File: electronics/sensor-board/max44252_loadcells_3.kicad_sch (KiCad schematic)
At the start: 21 parts

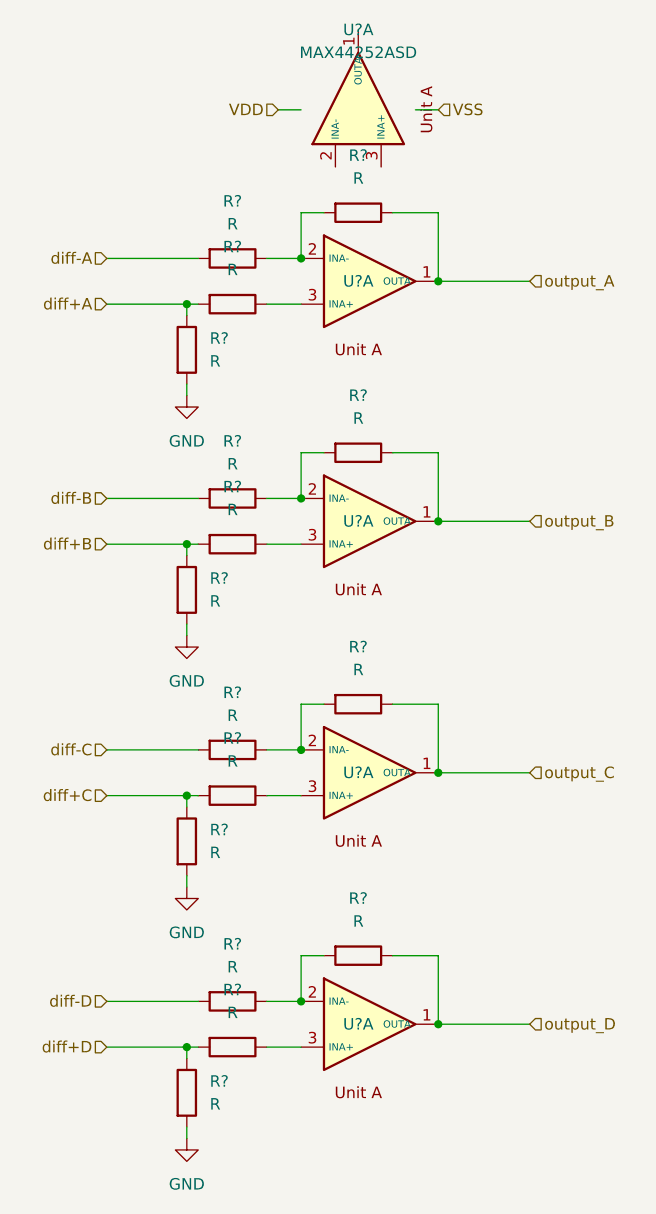
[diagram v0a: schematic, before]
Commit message: sensor-board edits
Finalized pressure and flow sensor circuits.
Reorganized schematics
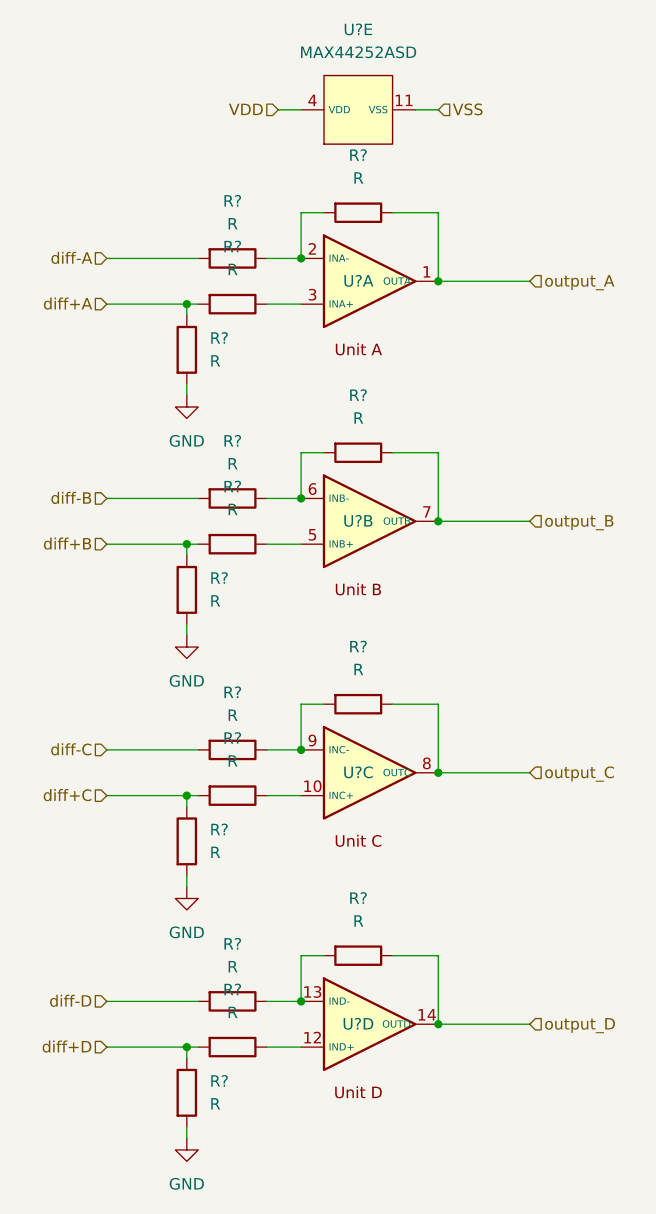
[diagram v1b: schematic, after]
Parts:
- removed R? (x16): R, symbol Device:R
- removed U? (x5): MAX44252ASD, symbol MAX44252ASD_Custom:MAX44252ASD
- added R? (x16): R, symbol Device:R
- added U? (x5): MAX44252ASD, symbol MAX44252ASD_Custom:MAX44252ASD
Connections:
- net GND: now also R?.2, R?.2, R?.2, R?.2
- net VDD: now also U?.4 (VDD)
- net VSS: now also U?.11 (VSS)
- net diff+A: now also R?.1, R?.2
- net diff+B: now also R?.1, R?.2
- net diff+C: now also R?.1, R?.2
- net diff+D: now also R?.1, R?.2
- net diff-A: now also R?.2
- net diff-B: now also R?.2
- net diff-C: now also R?.2
- net diff-D: now also R?.2
- net output_A: now also R?.1, U?.1 (OUTA)
- net output_B: now also R?.1, U?.7 (OUTB)
- net output_C: now also R?.1, U?.8 (OUTC)
- net output_D: now also R?.1, U?.14 (OUTD)
- new net: R?.1, U?.12 (IND+)
- new net: R?.1, U?.3 (INA+)
- new net: R?.1, U?.10 (INC+)
- new net: R?.1, R?.2, U?.13 (IND-)
- new net: R?.1, R?.2, U?.2 (INA-)
- new net: R?.1, R?.2, U?.9 (INC-)
- new net: R?.1, R?.2, U?.6 (INB-)
- new net: R?.1, U?.5 (INB+)
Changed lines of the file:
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@@
     (effects (font (size 1.27 1.27)) (justify left))
   )
-  (symbol (lib_id "power:GND") (at 134.62 76.2 0)
+  (symbol (lib_id "power:GND") (at 134.62 76.2 0) (unit 1)
     (in_bom yes) (on_board yes) (fields_autoplaced)
     (property "Reference" "#PWR?" (id 0) (at 134.62 82.55 0)
@@
     (pin "1")
   )
-  (symbol (lib_id "power:GND") (at 134.62 102.87 0)
+  (symbol (lib_id "power:GND") (at 134.62 102.87 0) (unit 1)
     (in_bom yes) (on_board yes) (fields_autoplaced)
     (property "Reference" "#PWR?" (id 0) (at 134.62 109.22 0)
@@
     (pin "1")
   )
-  (symbol (lib_id "power:GND") (at 134.62 130.81 0)
+  (symbol (lib_id "power:GND") (at 134.62 130.81 0) (unit 1)
     (in_bom yes) (on_board yes) (fields_autoplaced)
     (property "Reference" "#PWR?" (id 0) (at 134.62 137.16 0)
@@
     (pin "1")
   )
-  (symbol (lib_id "power:GND") (at 134.62 158.75 0)
+  (symbol (lib_id "power:GND") (at 134.62 158.75 0) (unit 1)
     (in_bom yes) (on_board yes) (fields_autoplaced)
     (property "Reference" "#PWR?" (id 0) (at 134.62 165.1 0)
@@
     (pin "1")
   )
-  (symbol (lib_id "Device:R") (at 134.62 71.12 0)
+  (symbol (lib_id "Device:R") (at 134.62 71.12 0) (unit 1)
     (in_bom yes) (on_board yes) (fields_autoplaced)
     (property "Reference" "R?" (id 0) (at 137.16 69.8499 0)
@@
     (pin "2")
   )
-  (symbol (lib_id "Device:R") (at 134.62 97.79 0)
+  (symbol (lib_id "Device:R") (at 134.62 97.79 0) (unit 1)
     (in_bom yes) (on_board yes) (fields_autoplaced)
     (property "Reference" "R?" (id 0) (at 137.16 96.5199 0)
@@
     (pin "2")
   )
-  (symbol (lib_id "Device:R") (at 134.62 125.73 0)
+  (symbol (lib_id "Device:R") (at 134.62 125.73 0) (unit 1)
     (in_bom yes) (on_board yes) (fields_autoplaced)
     (property "Reference" "R?" (id 0) (at 137.16 124.4599 0)
@@
     (pin "2")
   )
-  (symbol (lib_id "Device:R") (at 134.62 153.67 0)
+  (symbol (lib_id "Device:R") (at 134.62 153.67 0) (unit 1)
     (in_bom yes) (on_board yes) (fields_autoplaced)
     (property "Reference" "R?" (id 0) (at 137.16 152.3999 0)
@@
     (pin "2")
   )
-  (symbol (lib_id "Device:R") (at 139.7 60.96 270)
+  (symbol (lib_id "Device:R") (at 139.7 60.96 270) (unit 1)
     (in_bom yes) (on_board yes) (fields_autoplaced)
     (property "Reference" "R?" (id 0) (at 139.7 54.61 90))
@@
     (pin "2")
   )
-  (symbol (lib_id "Device:R") (at 139.7 66.04 270)
+  (symbol (lib_id "Device:R") (at 139.7 66.04 270) (unit 1)
     (in_bom yes) (on_board yes) (fields_autoplaced)
     (property "Reference" "R?" (id 0) (at 139.7 59.69 90))
@@
     (pin "2")
   )
-  (symbol (lib_id "Device:R") (at 139.7 87.63 270)
+  (symbol (lib_id "Device:R") (at 139.7 87.63 270) (unit 1)
     (in_bom yes) (on_board yes) (fields_autoplaced)
     (property "Reference" "R?" (id 0) (at 139.7 81.28 90))
@@
     (pin "2")
   )
-  (symbol (lib_id "Device:R") (at 139.7 92.71 270)
+  (symbol (lib_id "Device:R") (at 139.7 92.71 270) (unit 1)
     (in_bom yes) (on_board yes) (fields_autoplaced)
     (property "Reference" "R?" (id 0) (at 139.7 86.36 90))
@@
     (pin "2")
   )
-  (symbol (lib_id "Device:R") (at 139.7 115.57 270)
+  (symbol (lib_id "Device:R") (at 139.7 115.57 270) (unit 1)
     (in_bom yes) (on_board yes) (fields_autoplaced)
     (property "Reference" "R?" (id 0) (at 139.7 109.22 90))
@@
     (pin "2")
   )
-  (symbol (lib_id "Device:R") (at 139.7 120.65 270)
+  (symbol (lib_id "Device:R") (at 139.7 120.65 270) (unit 1)
     (in_bom yes) (on_board yes) (fields_autoplaced)
     (property "Reference" "R?" (id 0) (at 139.7 114.3 90))
@@
     (pin "2")
   )
-  (symbol (lib_id "Device:R") (at 139.7 143.51 270)
+  (symbol (lib_id "Device:R") (at 139.7 143.51 270) (unit 1)
     (in_bom yes) (on_board yes) (fields_autoplaced)
     (property "Reference" "R?" (id 0) (at 139.7 137.16 90))
@@
     (pin "2")
   )
-  (symbol (lib_id "Device:R") (at 139.7 148.59 270)
+  (symbol (lib_id "Device:R") (at 139.7 148.59 270) (unit 1)
     (in_bom yes) (on_board yes) (fields_autoplaced)
     (property "Reference" "R?" (id 0) (at 139.7 142.24 90))
@@
     (pin "2")
   )
-  (symbol (lib_id "Device:R") (at 153.67 55.88 270)
+  (symbol (lib_id "Device:R") (at 153.67 55.88 270) (unit 1)
     (in_bom yes) (on_board yes) (fields_autoplaced)
     (property "Reference" "R?" (id 0) (at 153.67 49.53 90))
@@
     (pin "2")
   )
-  (symbol (lib_id "Device:R") (at 153.67 82.55 270)
+  (symbol (lib_id "Device:R") (at 153.67 82.55 270) (unit 1)
     (in_bom yes) (on_board yes) (fields_autoplaced)
     (property "Reference" "R?" (id 0) (at 153.67 76.2 90))
@@
     (pin "2")
   )
-  (symbol (lib_id "Device:R") (at 153.67 110.49 270)
+  (symbol (lib_id "Device:R") (at 153.67 110.49 270) (unit 1)
     (in_bom yes) (on_board yes) (fields_autoplaced)
     (property "Reference" "R?" (id 0) (at 153.67 104.14 90))
@@
     (pin "2")
   )
-  (symbol (lib_id "Device:R") (at 153.67 138.43 270)
+  (symbol (lib_id "Device:R") (at 153.67 138.43 270) (unit 1)
     (in_bom yes) (on_board yes) (fields_autoplaced)
     (property "Reference" "R?" (id 0) (at 153.67 132.08 90))
@@
     (pin "2")
   )
-  (symbol (lib_id "MAX44252ASD_Custom:MAX44252ASD") (at 153.67 44.45 90)
+  (symbol (lib_id "MAX44252ASD_Custom:MAX44252ASD") (at 153.67 44.45 90) (unit 5)
     (in_bom yes) (on_board yes) (fields_autoplaced)
     (property "Reference" "U?" (id 0) (at 153.67 35.56 90))
@@
     (pin "4")
   )
-  (symbol (lib_id "MAX44252ASD_Custom:MAX44252ASD") (at 153.67 63.5 0)
+  (symbol (lib_id "MAX44252ASD_Custom:MAX44252ASD") (at 153.67 63.5 0) (unit 1)
     (in_bom yes) (on_board yes)
     (property "Reference" "U?" (id 0) (at 153.67 63.5 0))
@@
     (pin "3")
   )
-  (symbol (lib_id "MAX44252ASD_Custom:MAX44252ASD") (at 153.67 90.17 0)
+  (symbol (lib_id "MAX44252ASD_Custom:MAX44252ASD") (at 153.67 90.17 0) (unit 2)
     (in_bom yes) (on_board yes)
     (property "Reference" "U?" (id 0) (at 153.67 90.17 0))
@@
     (pin "7")
   )
-  (symbol (lib_id "MAX44252ASD_Custom:MAX44252ASD") (at 153.67 118.11 0)
+  (symbol (lib_id "MAX44252ASD_Custom:MAX44252ASD") (at 153.67 118.11 0) (unit 3)
     (in_bom yes) (on_board yes)
     (property "Reference" "U?" (id 0) (at 153.67 118.11 0))
@@
     (pin "9")
   )
-  (symbol (lib_id "MAX44252ASD_Custom:MAX44252ASD") (at 153.67 146.05 0)
+  (symbol (lib_id "MAX44252ASD_Custom:MAX44252ASD") (at 153.67 146.05 0) (unit 4)
     (in_bom yes) (on_board yes)
     (property "Reference" "U?" (id 0) (at 153.67 146.05 0))
